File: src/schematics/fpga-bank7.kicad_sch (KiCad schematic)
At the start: 1 part

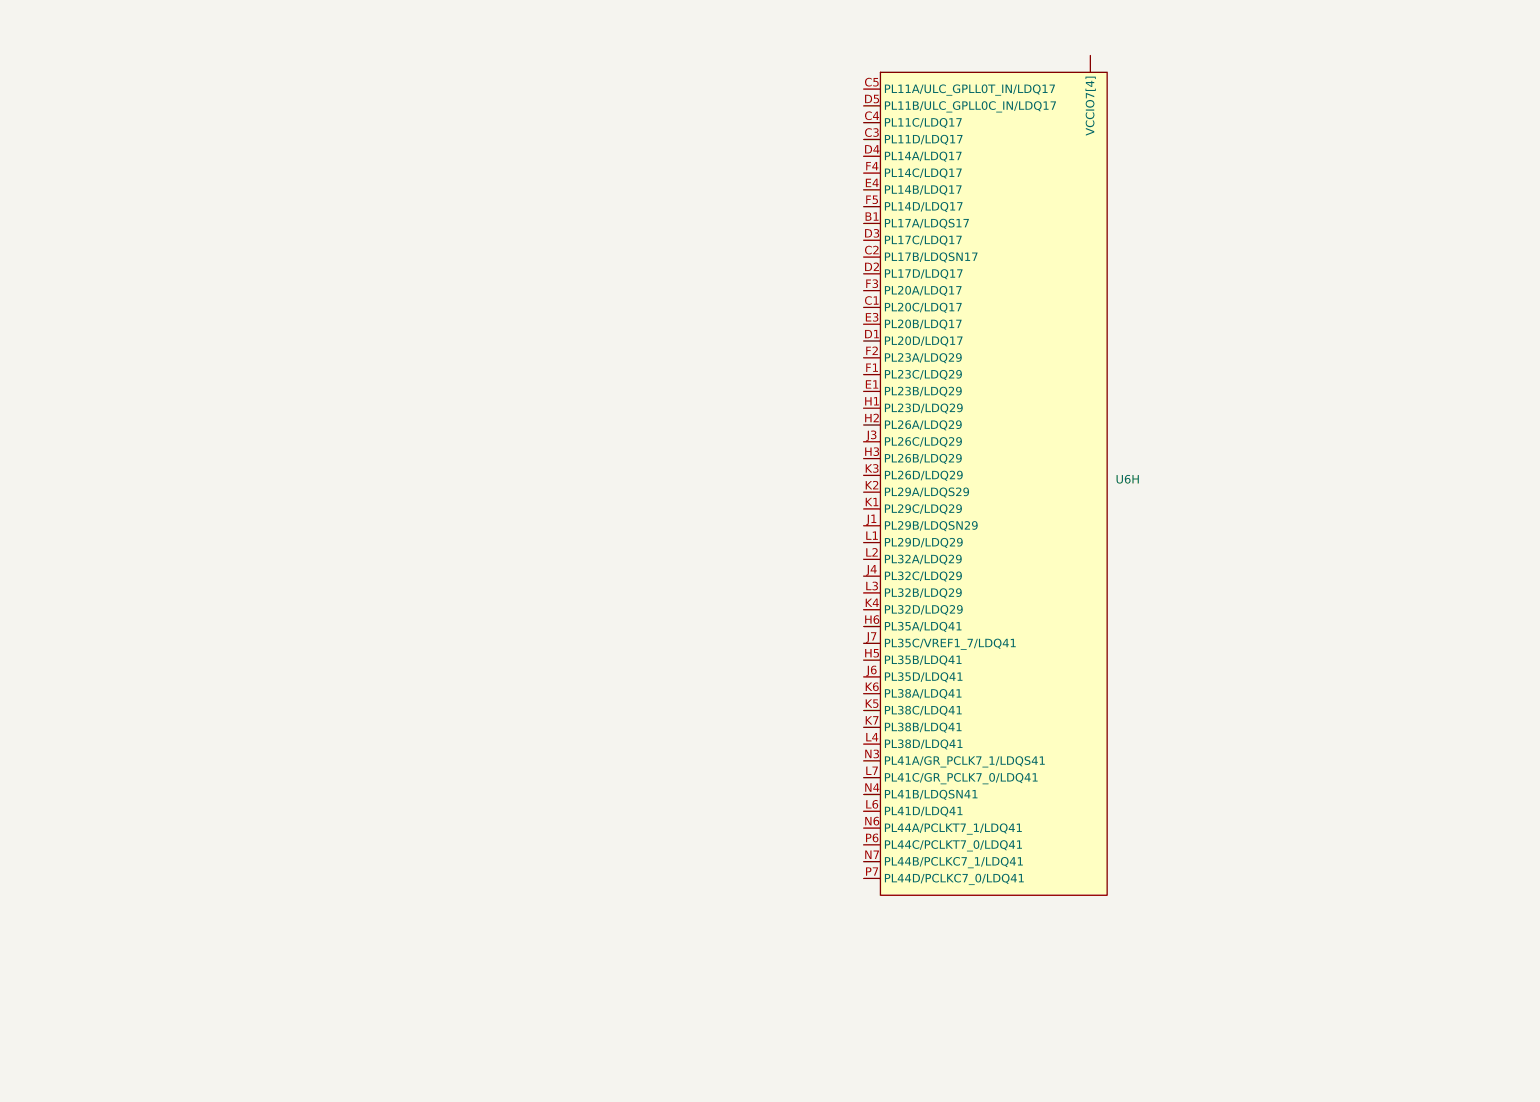
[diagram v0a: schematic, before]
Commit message: Draft connections between the FPGA and the memories
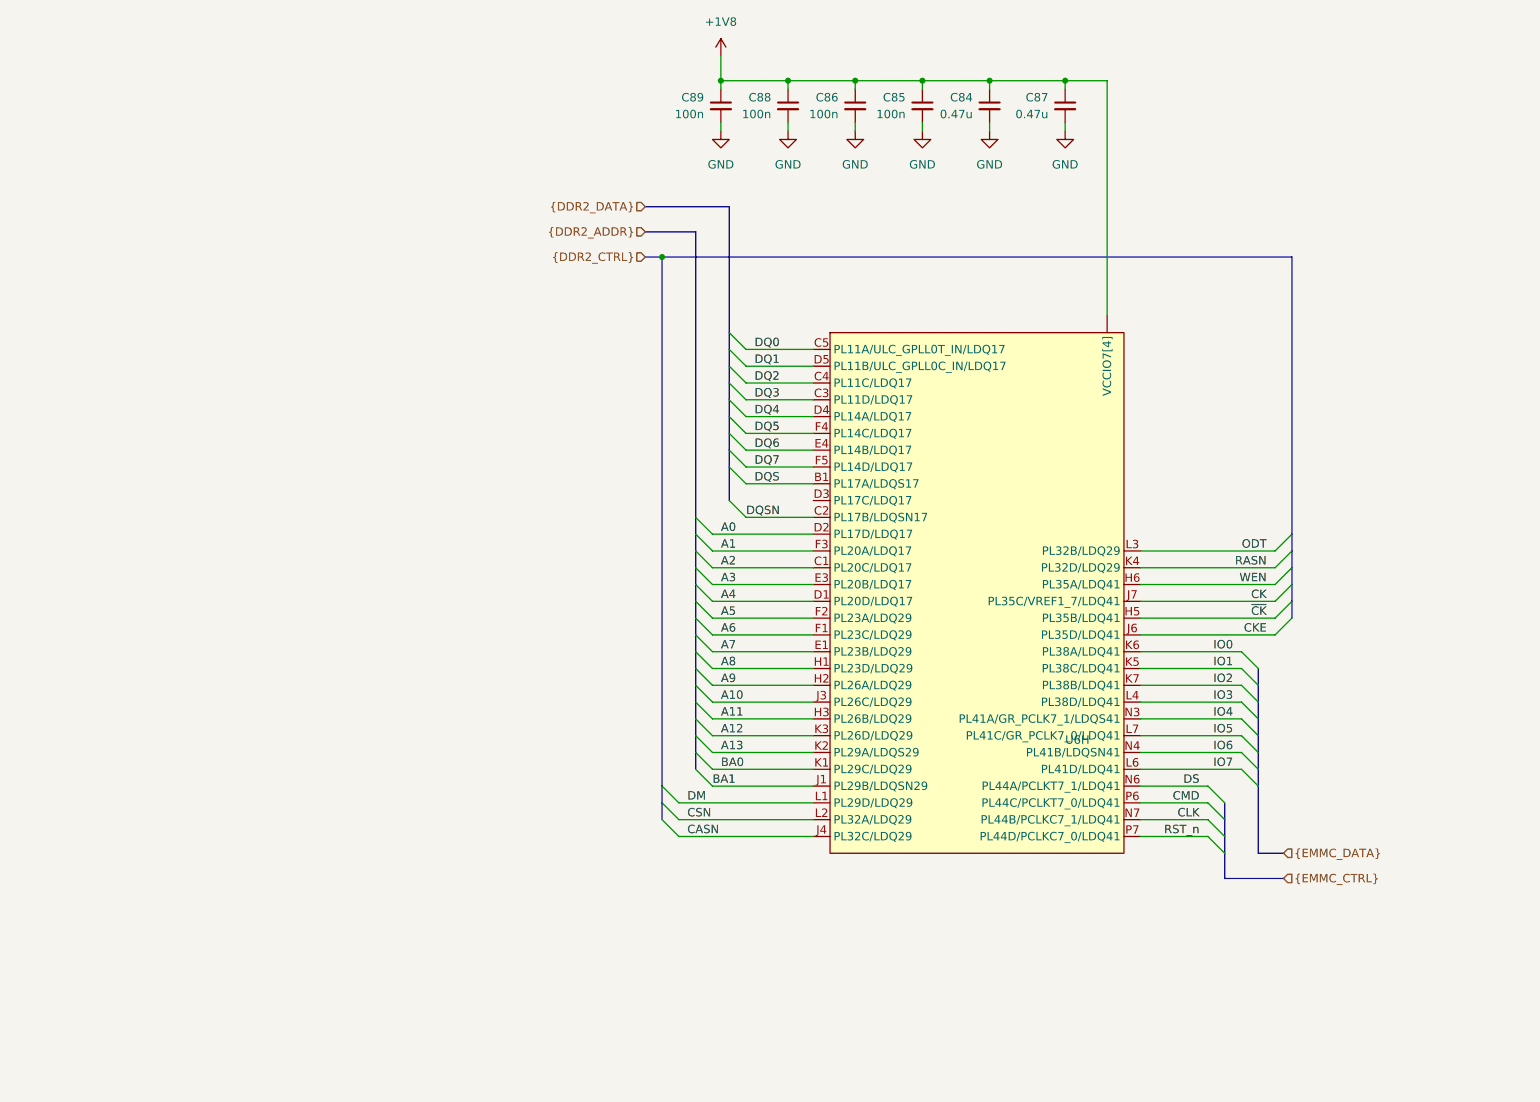
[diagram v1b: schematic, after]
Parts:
- added C84, C87: 0.47u, symbol Device:C_Small
- added C85, C86, C88, C89: 100n, symbol Device:C_Small
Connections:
- net DQS: now reaches U6.B1 (PL17A/LDQS17)
- net A2: now reaches U6.C1 (PL20C/LDQ17)
- net DQSN: now reaches U6.C2 (PL17B/LDQSN17)
- net DQ3: now reaches U6.C3 (PL11D/LDQ17)
- net DQ2: now reaches U6.C4 (PL11C/LDQ17)
- net DQ0: now reaches U6.C5 (PL11A/ULC_GPLL0T_IN/LDQ17)
- net A4: now reaches U6.D1 (PL20D/LDQ17)
- net A0: now reaches U6.D2 (PL17D/LDQ17)
- net DQ4: now reaches U6.D4 (PL14A/LDQ17)
- net DQ1: now reaches U6.D5 (PL11B/ULC_GPLL0C_IN/LDQ17)
- net A7: now reaches U6.E1 (PL23B/LDQ29)
- net A3: now reaches U6.E3 (PL20B/LDQ17)
- net DQ6: now reaches U6.E4 (PL14B/LDQ17)
- net A6: now reaches U6.F1 (PL23C/LDQ29)
- net A5: now reaches U6.F2 (PL23A/LDQ29)
- net A1: now reaches U6.F3 (PL20A/LDQ17)
- net DQ5: now reaches U6.F4 (PL14C/LDQ17)
- net DQ7: now reaches U6.F5 (PL14D/LDQ17)
- net A8: now reaches U6.H1 (PL23D/LDQ29)
- net A9: now reaches U6.H2 (PL26A/LDQ29)
- net A11: now reaches U6.H3 (PL26B/LDQ29)
- net ~{CK}: now reaches U6.H5 (PL35B/LDQ41)
- net WEN: now reaches U6.H6 (PL35A/LDQ41)
- net BA1: now reaches U6.J1 (PL29B/LDQSN29)
- net A10: now reaches U6.J3 (PL26C/LDQ29)
- net CASN: now reaches U6.J4 (PL32C/LDQ29)
- net CKE: now reaches U6.J6 (PL35D/LDQ41)
- net CK: now reaches U6.J7 (PL35C/VREF1_7/LDQ41)
- net BA0: now reaches U6.K1 (PL29C/LDQ29)
- net A13: now reaches U6.K2 (PL29A/LDQS29)
- net A12: now reaches U6.K3 (PL26D/LDQ29)
- net RASN: now reaches U6.K4 (PL32D/LDQ29)
- net IO1: now reaches U6.K5 (PL38C/LDQ41)
- net IO0: now reaches U6.K6 (PL38A/LDQ41)
- net IO2: now reaches U6.K7 (PL38B/LDQ41)
- net DM: now reaches U6.L1 (PL29D/LDQ29)
- net CSN: now reaches U6.L2 (PL32A/LDQ29)
- net ODT: now reaches U6.L3 (PL32B/LDQ29)
- net IO3: now reaches U6.L4 (PL38D/LDQ41)
- net IO7: now reaches U6.L6 (PL41D/LDQ41)
- net IO5: now reaches U6.L7 (PL41C/GR_PCLK7_0/LDQ41)
- net IO4: now reaches U6.N3 (PL41A/GR_PCLK7_1/LDQS41)
- net IO6: now reaches U6.N4 (PL41B/LDQSN41)
- net DS: now reaches U6.N6 (PL44A/PCLKT7_1/LDQ41)
- net CLK: now reaches U6.N7 (PL44B/PCLKC7_1/LDQ41)
- net CMD: now reaches U6.P6 (PL44C/PCLKT7_0/LDQ41)
- net RST_n: now reaches U6.P7 (PL44D/PCLKC7_0/LDQ41)
- net VCCIO7 renamed +1V8
- net +1V8: now also C84.1, C85.1, C86.1, C87.1, C88.1, C89.1
- new net GND: C84.2, C85.2, C86.2, C87.2, C88.2, C89.2
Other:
- moved on the sheet: U6H

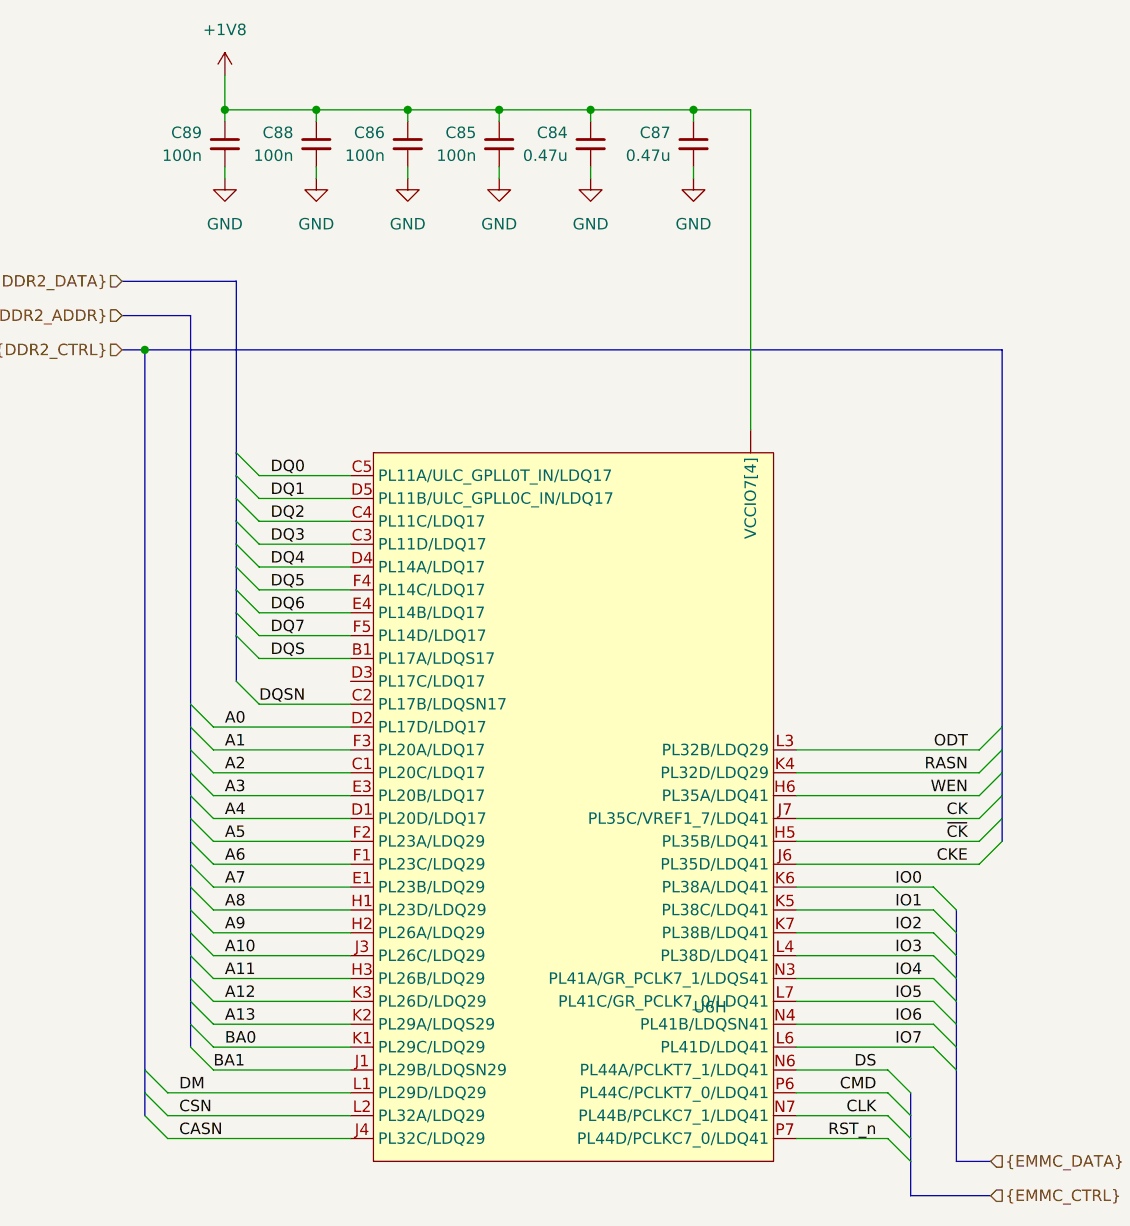
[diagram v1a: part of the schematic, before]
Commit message: Adds the clock oscillator
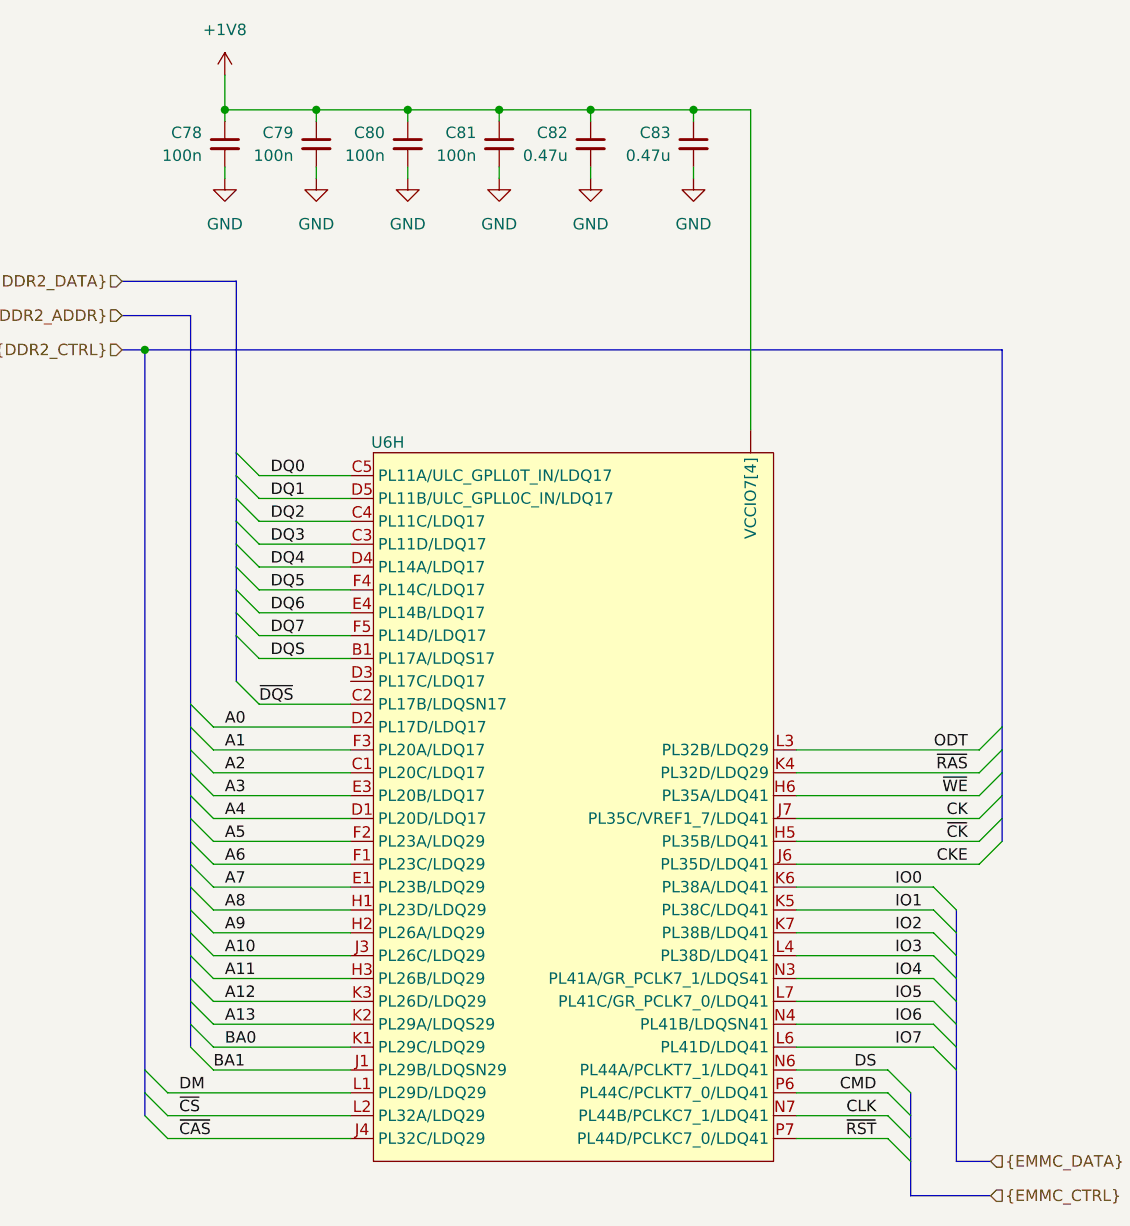
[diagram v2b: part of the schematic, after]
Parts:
- renumbered C89 to C78, C88 to C79, C86 to C80, C85 to C81, C84 to C82, C87 to C83
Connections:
- net CASN renamed ~{CAS}
- net CSN renamed ~{CS}
- net DQSN renamed ~{DQS}
- net RASN renamed ~{RAS}
- net RST_n renamed ~{RST}
- net WEN renamed ~{WE}
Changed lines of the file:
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@@
 		)
 	)
-	(label "CASN"
+	(label "~{CAS}"
 		(at 107.95 147.32 0)
 		(fields_autoplaced yes)
@@
 		)
 	)
-	(label "CSN"
+	(label "~{CS}"
 		(at 107.95 144.78 0)
 		(fields_autoplaced yes)
@@
 		)
 	)
-	(label "WEN"
+	(label "~{WE}"
 		(at 195.58 109.22 180)
 		(fields_autoplaced yes)
@@
 		)
 	)
-	(label "RASN"
+	(label "~{RAS}"
 		(at 195.58 106.68 180)
 		(fields_autoplaced yes)
@@
 		)
 	)
-	(label "DQSN"
+	(label "~{DQS}"
 		(at 116.84 99.06 0)
 		(fields_autoplaced yes)
@@
 		)
 	)
-	(label "RST_n"
+	(label "~{RST}"
 		(at 185.42 147.32 180)
 		(fields_autoplaced yes)
@@
 		(dnp no)
 		(fields_autoplaced yes)
-		(property "Reference" "#PWR090"
+		(property "Reference" "#PWR060"
 			(at 113.03 33.02 0)
 			(effects
@@
 			(project "ecap5-bsom"
 				(path "/c5fd18a3-9aa0-4151-b6e0-94da3d606686/9ec64d27-698a-408d-bb9c-7e381193a80d/9a63a507-5244-41c3-8e77-e9299b12167a"
-					(reference "#PWR090")
+					(reference "#PWR060")
 					(unit 1)
 				)
@@
 		(dnp no)
 		(fields_autoplaced yes)
-		(property "Reference" "#PWR093"
+		(property "Reference" "#PWR063"
 			(at 133.35 46.99 0)
 			(effects
@@
 			(project "ecap5-bsom"
 				(path "/c5fd18a3-9aa0-4151-b6e0-94da3d606686/9ec64d27-698a-408d-bb9c-7e381193a80d/9a63a507-5244-41c3-8e77-e9299b12167a"
-					(reference "#PWR093")
+					(reference "#PWR063")
 					(unit 1)
 				)
@@
 		(dnp no)
 		(fields_autoplaced yes)
-		(property "Reference" "C87"
+		(property "Reference" "C83"
 			(at 162.56 35.5662 0)
 			(effects
@@
 			(project "ecap5-bsom"
 				(path "/c5fd18a3-9aa0-4151-b6e0-94da3d606686/9ec64d27-698a-408d-bb9c-7e381193a80d/9a63a507-5244-41c3-8e77-e9299b12167a"
-					(reference "C87")
+					(reference "C83")
 					(unit 1)
 				)
@@
 		(dnp no)
 		(fields_autoplaced yes)
-		(property "Reference" "#PWR095"
+		(property "Reference" "#PWR062"
 			(at 123.19 46.99 0)
 			(effects
@@
 			(project "ecap5-bsom"
 				(path "/c5fd18a3-9aa0-4151-b6e0-94da3d606686/9ec64d27-698a-408d-bb9c-7e381193a80d/9a63a507-5244-41c3-8e77-e9299b12167a"
-					(reference "#PWR095")
+					(reference "#PWR062")
 					(unit 1)
 				)
@@
 		(dnp no)
 		(fields_autoplaced yes)
-		(property "Reference" "#PWR092"
+		(property "Reference" "#PWR064"
 			(at 143.51 46.99 0)
 			(effects
@@
 			(project "ecap5-bsom"
 				(path "/c5fd18a3-9aa0-4151-b6e0-94da3d606686/9ec64d27-698a-408d-bb9c-7e381193a80d/9a63a507-5244-41c3-8e77-e9299b12167a"
-					(reference "#PWR092")
+					(reference "#PWR064")
 					(unit 1)
 				)
@@
 		(dnp no)
 		(fields_autoplaced yes)
-		(property "Reference" "#PWR096"
+		(property "Reference" "#PWR061"
 			(at 113.03 46.99 0)
 			(effects
@@
 			(project "ecap5-bsom"
 				(path "/c5fd18a3-9aa0-4151-b6e0-94da3d606686/9ec64d27-698a-408d-bb9c-7e381193a80d/9a63a507-5244-41c3-8e77-e9299b12167a"
-					(reference "#PWR096")
+					(reference "#PWR061")
 					(unit 1)
 				)
@@
 		(on_board yes)
 		(dnp no)
-		(fields_autoplaced yes)
 		(property "Reference" "U6"
-			(at 165.1 132.7149 0)
+			(at 129.286 69.9769 0)
 			(effects
 				(font
@@
 		(dnp no)
 		(fields_autoplaced yes)
-		(property "Reference" "C84"
+		(property "Reference" "C82"
 			(at 151.13 35.5662 0)
 			(effects
@@
 			(project "ecap5-bsom"
 				(path "/c5fd18a3-9aa0-4151-b6e0-94da3d606686/9ec64d27-698a-408d-bb9c-7e381193a80d/9a63a507-5244-41c3-8e77-e9299b12167a"
-					(reference "C84")
+					(reference "C82")
 					(unit 1)
 				)
@@
 		(dnp no)
 		(fields_autoplaced yes)
-		(property "Reference" "#PWR094"
+		(property "Reference" "#PWR066"
 			(at 165.1 46.99 0)
 			(effects
@@
 			(project "ecap5-bsom"
 				(path "/c5fd18a3-9aa0-4151-b6e0-94da3d606686/9ec64d27-698a-408d-bb9c-7e381193a80d/9a63a507-5244-41c3-8e77-e9299b12167a"
-					(reference "#PWR094")
+					(reference "#PWR066")
 					(unit 1)
 				)
@@
 		(dnp no)
 		(fields_autoplaced yes)
-		(property "Reference" "C88"
+		(property "Reference" "C79"
 			(at 120.65 35.5662 0)
 			(effects
@@
 			(project "ecap5-bsom"
 				(path "/c5fd18a3-9aa0-4151-b6e0-94da3d606686/9ec64d27-698a-408d-bb9c-7e381193a80d/9a63a507-5244-41c3-8e77-e9299b12167a"
-					(reference "C88")
+					(reference "C79")
 					(unit 1)
 				)
@@
 		(dnp no)
 		(fields_autoplaced yes)
-		(property "Reference" "C86"
+		(property "Reference" "C80"
 			(at 130.81 35.5662 0)
 			(effects
@@
 			(project "ecap5-bsom"
 				(path "/c5fd18a3-9aa0-4151-b6e0-94da3d606686/9ec64d27-698a-408d-bb9c-7e381193a80d/9a63a507-5244-41c3-8e77-e9299b12167a"
-					(reference "C86")
+					(reference "C80")
 					(unit 1)
 				)
@@
 		(dnp no)
 		(fields_autoplaced yes)
-		(property "Reference" "#PWR091"
+		(property "Reference" "#PWR065"
 			(at 153.67 46.99 0)
 			(effects
@@
 			(project "ecap5-bsom"
 				(path "/c5fd18a3-9aa0-4151-b6e0-94da3d606686/9ec64d27-698a-408d-bb9c-7e381193a80d/9a63a507-5244-41c3-8e77-e9299b12167a"
-					(reference "#PWR091")
+					(reference "#PWR065")
 					(unit 1)
 				)
@@
 		(dnp no)
 		(fields_autoplaced yes)
-		(property "Reference" "C89"
+		(property "Reference" "C78"
 			(at 110.49 35.5662 0)
 			(effects
@@
 			(project "ecap5-bsom"
 				(path "/c5fd18a3-9aa0-4151-b6e0-94da3d606686/9ec64d27-698a-408d-bb9c-7e381193a80d/9a63a507-5244-41c3-8e77-e9299b12167a"
-					(reference "C89")
+					(reference "C78")
 					(unit 1)
 				)
@@
 		(dnp no)
 		(fields_autoplaced yes)
-		(property "Reference" "C85"
+		(property "Reference" "C81"
 			(at 140.97 35.5662 0)
 			(effects
@@
 			(project "ecap5-bsom"
 				(path "/c5fd18a3-9aa0-4151-b6e0-94da3d606686/9ec64d27-698a-408d-bb9c-7e381193a80d/9a63a507-5244-41c3-8e77-e9299b12167a"
-					(reference "C85")
+					(reference "C81")
 					(unit 1)
 				)
